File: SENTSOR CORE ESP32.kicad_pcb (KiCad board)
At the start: 2 copper layers, 35.6 x 35.6 mm, 84 parts, among them J1 HYC80-TF08-375, J2 Conn_01x10_Pin, J3 Conn_01x10_Pin, J4 Conn_01x10_Pin, J5 JST_PH 2.0mm, J6 TYPEC-304S-ACP16, Q1 SL8205S, Q2 CJ2301, Q3 UMH3N, SW1 SW_Push, SW2 SW_Push, U1 ESP32-WROOM-32UE, U2 DS3231MZ, U3 XC6220B331MR, U4 XC6220B331MR, U5 BQ27441DRZR-G1B, U6 CN3165, U7 DW01A, U8 USBLC6-2SC6, U9 CH340K

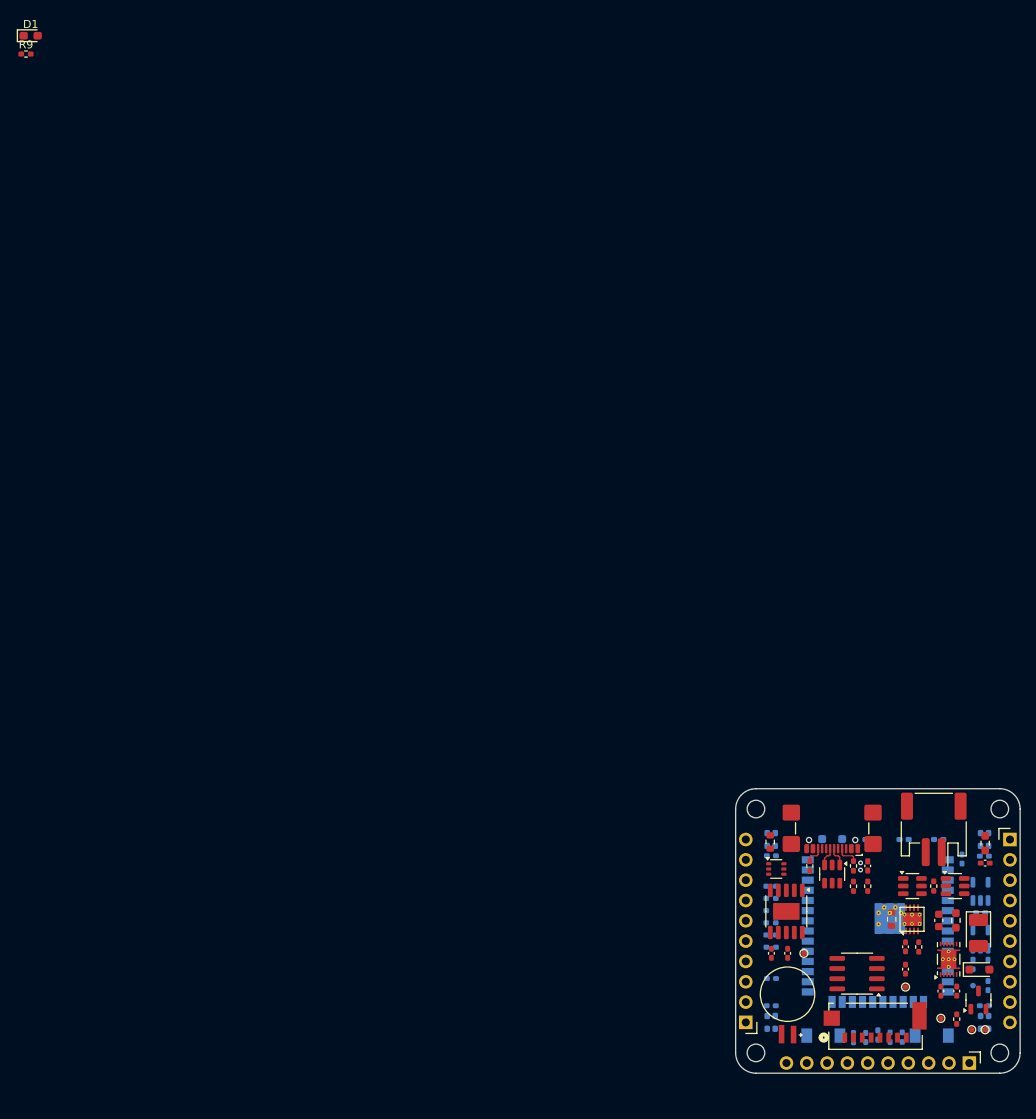
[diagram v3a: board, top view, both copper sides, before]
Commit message: add board layout
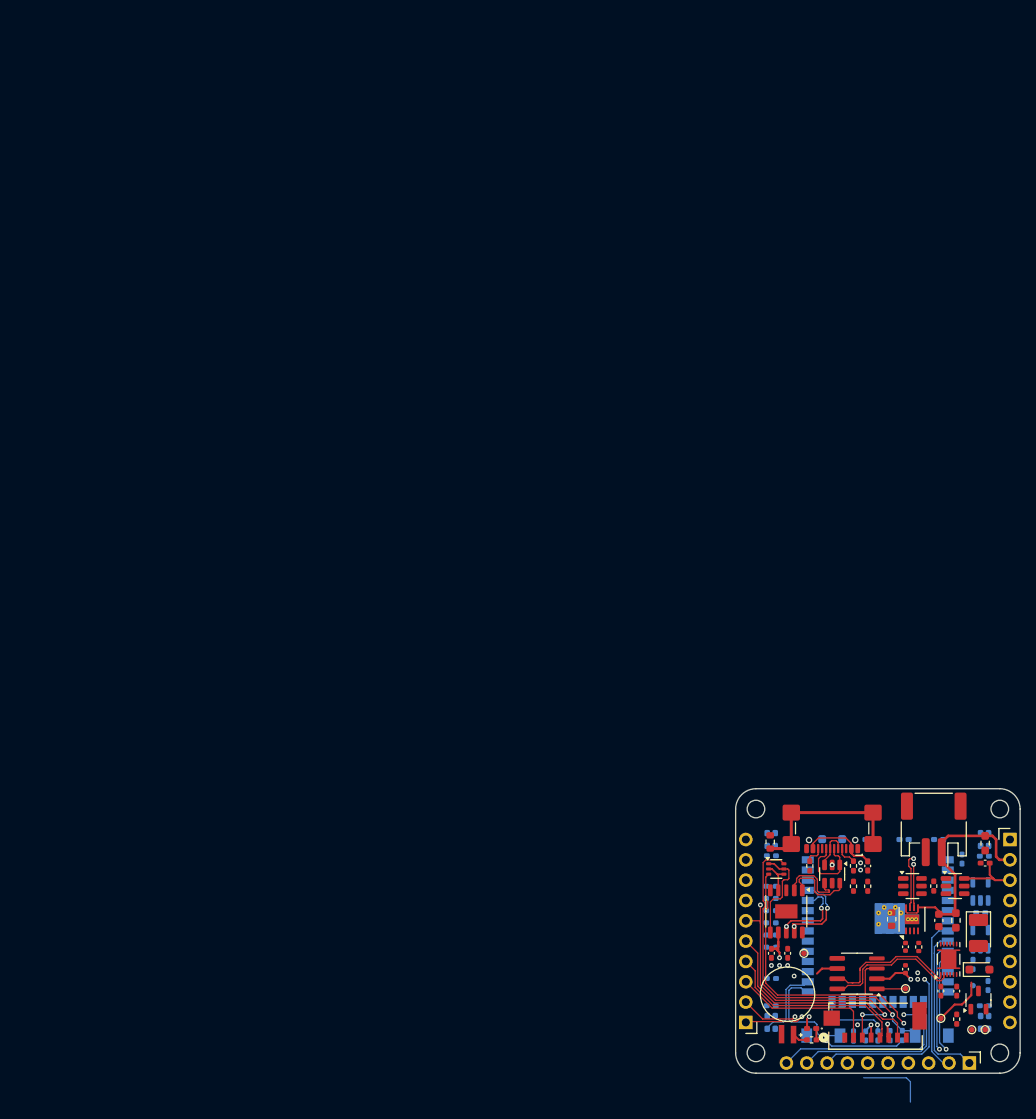
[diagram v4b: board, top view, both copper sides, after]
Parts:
- C18, C4: footprint Capacitor_SMD:C_0402_1005Metric_Pad0.74x0.62mm_HandSolder -> Capacitor_SMD:C_0402_1005Metric
- D1: footprint Diode_SMD:D_0603_1608Metric_Pad1.05x0.95mm_HandSolder -> Diode_SMD:D_0402_1005Metric_Pad0.77x0.64mm_HandSolder
- R12: footprint Resistor_SMD:R_0402_1005Metric_Pad0.72x0.64mm_HandSolder -> Resistor_SMD:R_0402_1005Metric
- moved D1 157.9 mm to (99.3, 124.9), turned to 180 degrees
- moved R9 157.6 mm to (99.3, 126.3)
- moved C3 0.20 mm to (106.1, 125.8)
- moved R1 0.20 mm to (110.7, 125.8)
- moved R16 0.20 mm to (109.1, 125.8)
- moved R2 0.20 mm to (104.6, 125.8)
- moved TP4 0.20 mm to (111.1, 119.9)
- moved D3 0.12 mm to (107.6, 125.8)
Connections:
- Q3 pad 2: /DRT -> /DTR
- Q3 pad 4: /DRT -> /DTR
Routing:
- net /BOOT: track 0.00 -> 52.5 mm, vias 0 -> 1
- net /RST: track 0.00 -> 40.5 mm, vias 0 -> 1
- net /SPI_MOSI: track 0.00 -> 34.9 mm, vias 0 -> 3
- net VBAT0+: track 0.00 -> 29.0 mm
- net /SPI_MISO: track 0.00 -> 27.4 mm
- net /I2C_SCL: track 0.00 -> 24.9 mm, vias 0 -> 1
- net /JTAG_TDI: track 0.00 -> 24.3 mm, vias 0 -> 1
- net /I2C_SDA: track 0.00 -> 24.3 mm, vias 0 -> 1
- net /SPI_SCK: track 0.00 -> 23.4 mm
- net /JTAG_TCK: track 0.00 -> 22.7 mm
- net /JTAG_TMS: track 0.00 -> 22.3 mm, vias 0 -> 1
- net Net-(J6-SHIELD): track 0.00 -> 21.0 mm
- net /IO33: track 0.00 -> 19.9 mm
- net /IO32: track 0.00 -> 19.3 mm
- net /SPI_SS: track 0.00 -> 18.3 mm
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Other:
- copper layers 2 -> 4
- rule pad_to_mask_clearance: 0 -> 0.0254

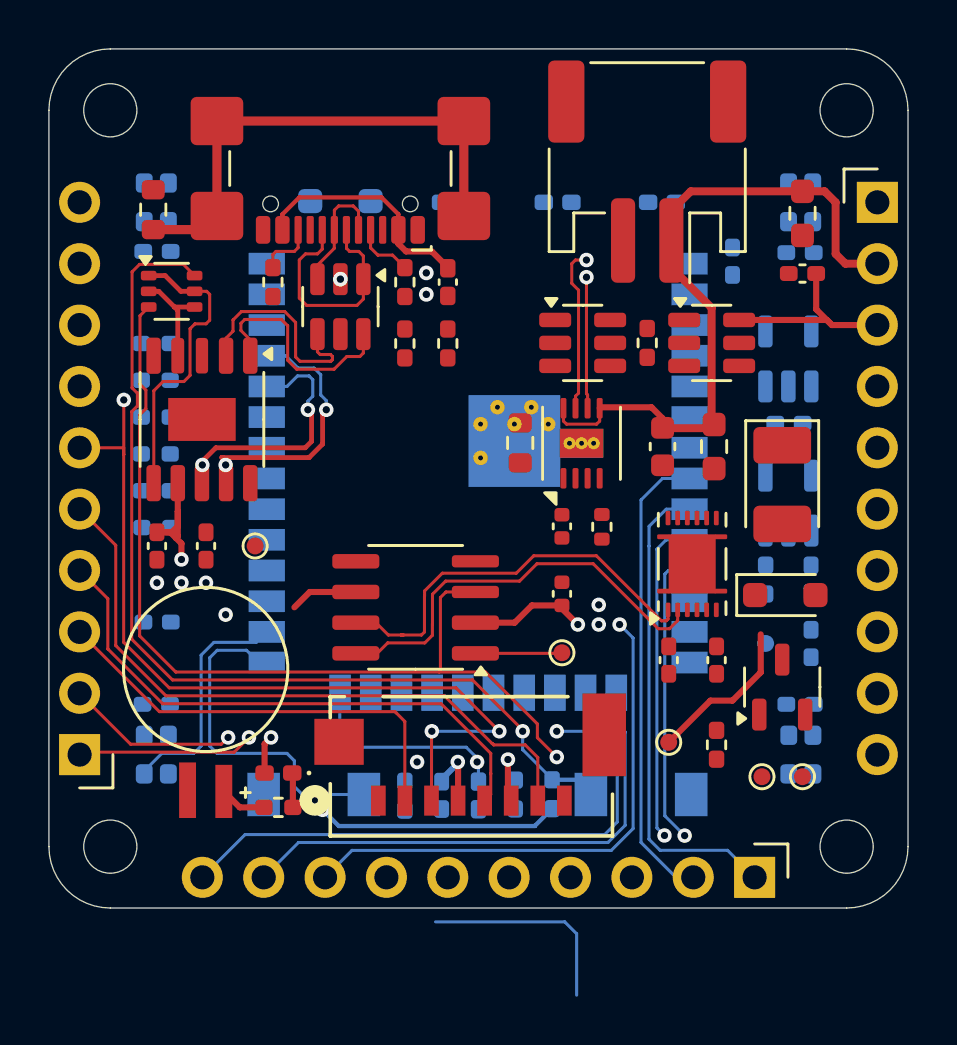
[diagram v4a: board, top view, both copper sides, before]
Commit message: add board layout 85%
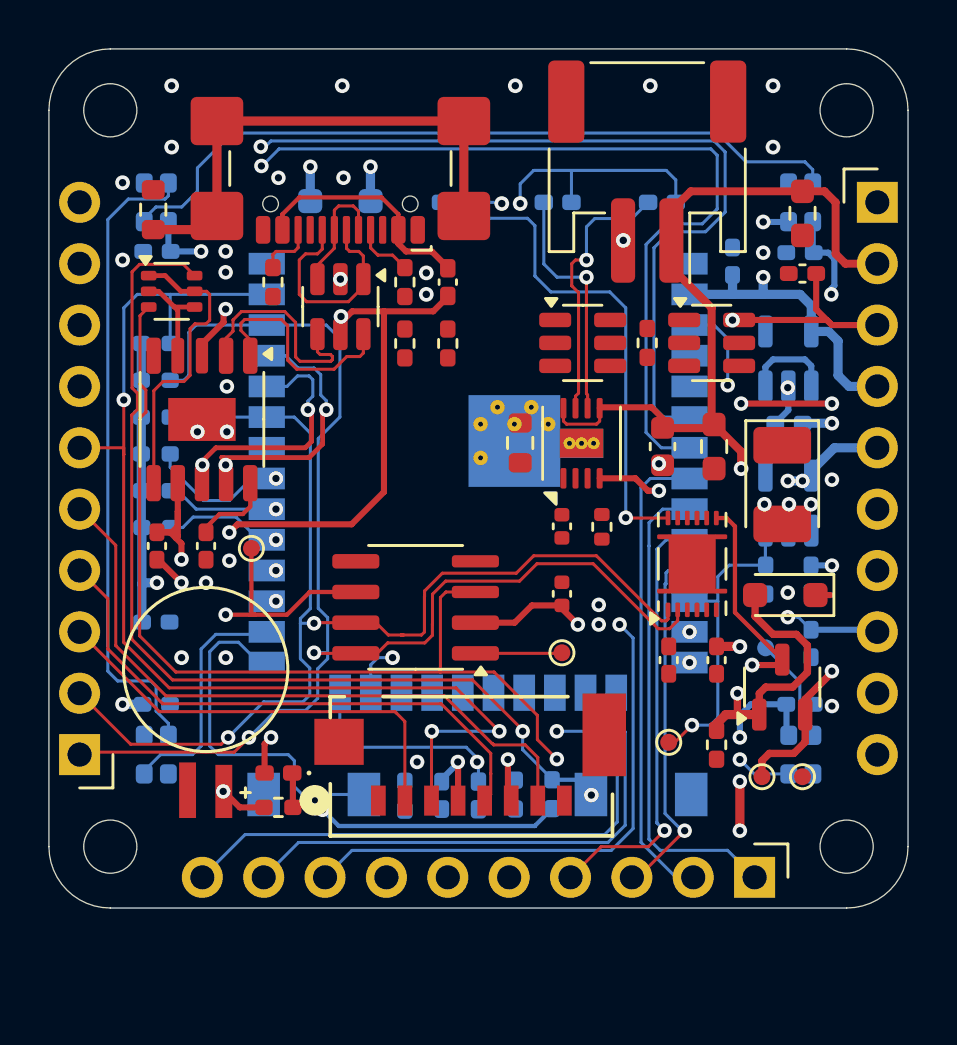
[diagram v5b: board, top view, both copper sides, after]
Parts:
- moved TP1 0.18 mm to (98.2, 115.6)
- moved TP2 0.18 mm to (119.5, 119.7)
- moved C6 0.05 mm to (94.3, 118.6)
- turned C14 to 180 degrees
- turned C15 to 0 degrees
- turned D8 to 180 degrees
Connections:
- R11 pad 1: Net-(U3-CE) -> /LDO_EN
- TP3 pad 1: Net-(U3-CE) -> /LDO_EN
- U3 pad 3: Net-(U3-CE) -> /LDO_EN
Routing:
- net VIN0: track 0.00 -> 73.0 mm, vias 0 -> 5
- net +3V30: track 10.1 -> 68.7 mm, vias 1 -> 4
- net /I35: track 0.00 -> 44.3 mm, vias 0 -> 1
- net /I34: track 0.00 -> 43.2 mm, vias 0 -> 1
- net /RST: track 40.5 -> 75.0 mm, vias 1 -> 4
- net VUSB: track 5.75 -> 36.8 mm, vias 1 -> 4
- net Net-(D5-DOUT): track 0.00 -> 31.0 mm
- net /I2C_SCL: track 24.9 -> 55.5 mm, vias 1 -> 2
- net +3V3: track 9.17 -> 37.0 mm, vias 4 -> 10
- net Net-(D6-DOUT): track 0.00 -> 26.8 mm, vias 0 -> 2
- net Net-(D4-DOUT): track 0.00 -> 26.6 mm
- net /I2C_SDA: track 24.3 -> 47.9 mm, vias 1 -> 2
- net /LED: track 8.98 -> 30.6 mm
- net /GPOUT: track 0.00 -> 21.1 mm, vias 0 -> 1
- net /IO17: track 0.00 -> 20.1 mm, vias 0 -> 1
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
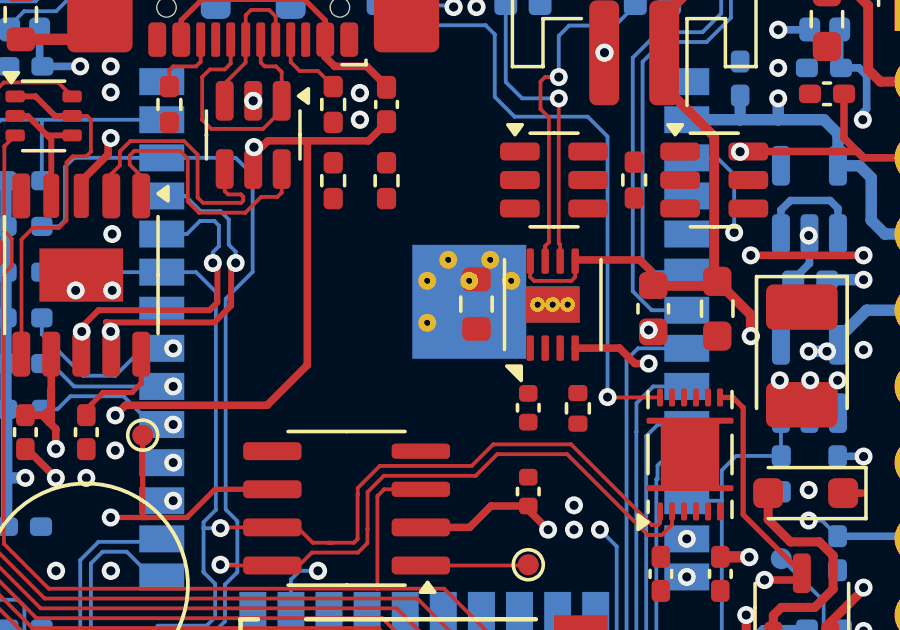
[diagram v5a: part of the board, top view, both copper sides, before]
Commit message: add board layout 85%
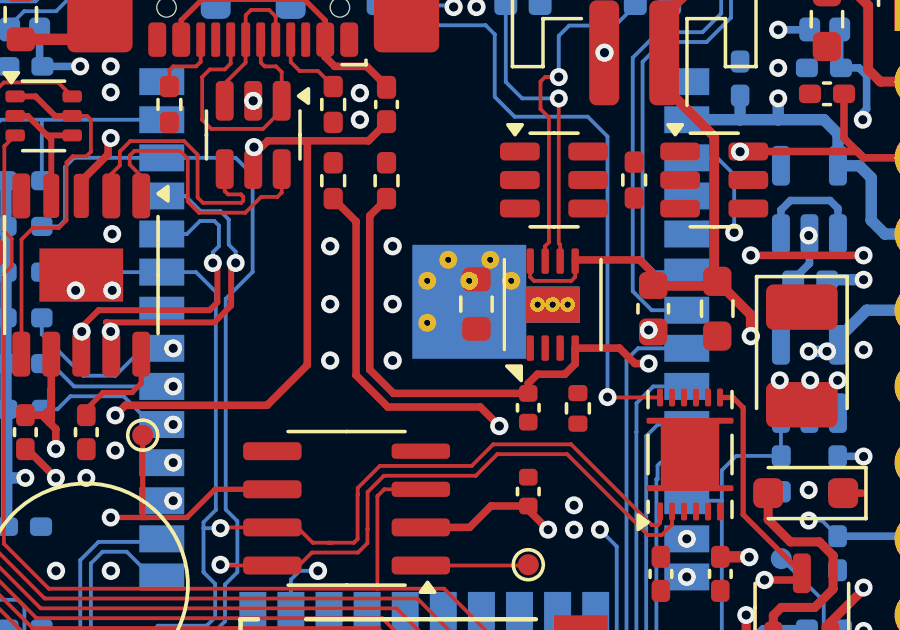
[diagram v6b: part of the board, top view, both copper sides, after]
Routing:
- net VIN0: track 73.0 -> 87.2 mm
- net VBAT+: track 19.7 -> 31.4 mm, vias 2 -> 3
- net GND: vias 36 -> 42
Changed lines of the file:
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@@
 	)
 	(via
+		(at 104.4704 111.2268)
+		(size 0.6096)
+		(drill 0.3048)
+		(layers "F.Cu" "B.Cu")
+		(free yes)
+		(net 1)
+	)
+	(via
 		(at 105.08 124.4348)
 		(size 0.6)
@@
 	)
 	(via
+		(at 104.4704 109.2964)
+		(size 0.6096)
+		(drill 0.3048)
+		(layers "F.Cu" "B.Cu")
+		(free yes)
+		(net 1)
+	)
+	(via
 		(at 95.3264 117.018)
 		(size 0.6)
@@
 	)
 	(via
+		(at 106.5532 113.1064)
+		(size 0.6096)
+		(drill 0.3048)
+		(layers "F.Cu" "B.Cu")
+		(free yes)
+		(net 1)
+	)
+	(via
 		(at 97.1552 105.6896)
 		(size 0.6)
@@
 	)
 	(via
+		(at 106.5532 111.2268)
+		(size 0.6096)
+		(drill 0.3048)
+		(layers "F.Cu" "B.Cu")
+		(free yes)
+		(net 1)
+	)
+	(via
 		(at 119.812 98.984)
 		(size 0.6096)
@@
 	)
 	(via
+		(at 106.5532 109.2964)
+		(size 0.6096)
+		(drill 0.3048)
+		(layers "F.Cu" "B.Cu")
+		(free yes)
+		(net 1)
+	)
+	(via
 		(at 97.206 108.89)
 		(size 0.6)
@@
 	)
 	(via
+		(at 104.4704 113.1064)
+		(size 0.6096)
+		(drill 0.3048)
+		(layers "F.Cu" "B.Cu")
+		(free yes)
+		(net 1)
+	)
+	(via
 		(at 97.3076 116.1036)
 		(size 0.6)
@@
 	)
 	(segment
+		(start 111.3792 113.5636)
+		(end 112.2936 113.5636)
+		(width 0.254)
+		(layer "F.Cu")
+		(net 12)
+	)
+	(segment
+		(start 111.0744 114.2012)
+		(end 111.0744 113.8684)
+		(width 0.254)
+		(layer "F.Cu")
+		(net 12)
+	)
+	(segment
+		(start 106.5812 114.2012)
+		(end 111.0744 114.2012)
+		(width 0.254)
+		(layer "F.Cu")
+		(net 12)
+	)
+	(segment
 		(start 117.4752 123.1261)
 		(end 117.4752 122.86)
@@
 	)
 	(segment
+		(start 105.7912 113.4112)
+		(end 106.5812 114.2012)
+		(width 0.254)
+		(layer "F.Cu")
+		(net 12)
+	)
+	(segment
 		(start 117.4752 122.86)
 		(end 117.8617 122.4735)
@@
 	)
 	(segment
+		(start 111.0744 113.8684)
+		(end 111.3792 113.5636)
+		(width 0.254)
+		(layer "F.Cu")
+		(net 12)
+	)
+	(segment
 		(start 120.6248 121.336)
 		(end 119.5072 121.336)
@@
 	)
 	(segment
+		(start 112.2936 113.5636)
+		(end 112.637 113.2202)
+		(width 0.254)
+		(layer "F.Cu")
+		(net 12)
+	)
+	(segment
+		(start 105.7912 108.2804)
+		(end 105.7912 113.4112)
+		(width 0.254)
+		(layer "F.Cu")
+		(net 12)
+	)
+	(segment
 		(start 117.8617 122.4735)
 		(end 118.3388 122.4735)
@@
 	)
 	(segment
+		(start 106.35 107.7216)
+		(end 105.7912 108.2804)
+		(width 0.254)
+		(layer "F.Cu")
+		(net 12)
+	)
+	(segment
 		(start 119.243 121.6002)
 		(end 119.243 122.4735)
@@
 		(net 12)
 	)
+	(segment
+		(start 112.637 113.2202)
+		(end 112.637 112.693)
+		(width 0.254)
+		(layer "F.Cu")
+		(net 12)
+	)
+	(segment
+		(start 106.35 107.7095)
+		(end 106.35 107.7216)
+		(width 0.254)
+		(layer "F.Cu")
+		(net 12)
+	)
 	(via
 		(at 103.1496 99.7968)
@@
 	)
 	(segment
+		(start 105.334 113.597467)
+		(end 106.392733 114.6562)
+		(width 0.254)
+		(layer "F.Cu")
+		(net 63)
+	)
+	(segment
 		(start 117.894 114.338)
 		(end 118.2372 114.6812)
@@
 	)
 	(segment
+		(start 106.392733 114.6562)
+		(end 109.4746 114.6562)
+		(width 0.254)
+		(layer "F.Cu")
+		(net 63)
+	)
+	(segment
+		(start 105.334 108.4715)
+		(end 105.334 113.597467)
+		(width 0.254)
+		(layer "F.Cu")
+		(net 63)
+	)
+	(segment
 		(start 119.9699 120.4216)
 		(end 120.193 120.1985)
@@
 	)
 	(segment
+		(start 104.572 107.7095)
+		(end 105.334 108.4715)
+		(width 0.254)
+		(layer "F.Cu")
+		(net 63)
+	)
+	(segment
+		(start 109.4746 114.6562)
+		(end 110.1092 115.2908)
+		(width 0.254)
+		(layer "F.Cu")
+		(net 63)
+	)
+	(segment
 		(start 118.2372 114.6812)
 		(end 118.2372 118.2427)
@@
 		(size 0.6096)
 		(drill 0.3048)
+		(layers "F.Cu" "B.Cu")
+		(free yes)
+		(net 63)
+	)
+	(via
+		(at 110.1092 115.2908)
+		(size 0.6096)
+		(drill 0.3048)

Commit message: add board layout 90%
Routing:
- net VBAT-: track 15.6 -> 23.7 mm
- net Net-(D2-A): track 1.39 -> 9.49 mm
- net VIN: track 18.7 -> 26.0 mm
- net Net-(D10-A): track 9.90 -> 16.8 mm
- net Net-(U7-VCC): track 0.00 -> 6.43 mm
- net Net-(U5-BIN): track 0.00 -> 4.37 mm
- net Net-(U6-ISET): track 0.00 -> 4.15 mm
- net VBAT0+: track 39.6 -> 43.7 mm
- net Net-(Q1-G2): track 0.00 -> 3.97 mm
- net Net-(U5-V_{DD}): track 0.00 -> 2.73 mm
- net /I34: track 43.2 -> 45.4 mm
- net /I35: track 44.3 -> 46.5 mm
- net VBAT+: track 31.4 -> 33.5 mm
- net GND: track 7.26 -> 9.24 mm, vias 42 -> 61
- net Net-(U7-CS): track 0.00 -> 1.78 mm
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
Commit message: add board layout 100% first
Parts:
- added G***: LOGO, LOGO, F.Cu at (101.7, 111.1)
- H1, H2, H3, H4: footprint MountingHole:MountingHole_2.2mm_M2 -> MountingHole:MountingHole_2.2mm_M2_Pad_Via
- turned R2 to 90 degrees
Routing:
- net GND: track 9.24 -> 23.3 mm
- net +3V3: track 37.0 -> 41.9 mm
- net VBAT+: track 33.5 -> 38.0 mm
- net Net-(Q1-G1): track 0.00 -> 4.19 mm
- net VIN: track 26.0 -> 29.1 mm
- net /BOOT: track 70.8 -> 73.3 mm, vias 1 -> 2
- net Net-(D3-A): track 0.00 -> 1.53 mm
- net VBAT0+: track 43.7 -> 45.2 mm
- net VIN0: track 87.4 -> 86.1 mm
- net /I2C_SCL: track 55.5 -> 54.4 mm
- net +3V30: track 68.7 -> 69.3 mm
- added copper zone on In1.Cu, net +3V3
- added copper zone on B.Cu, net GND
- added copper zone on F.Cu, net GND
- added copper zone on In2.Cu, net GND
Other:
- board text added: "+"
- board text added: "-"
- board text added: "1S LIPO"
- board text added: "32KHZ"
- board text added: "ALRM"
- board text added: "BOOT"
- board text added: "CHGR"
- board text added: "ESP32-WROOM-32UE"
- board text added: "FULL"
- board text added: "ISET"
- board text added: "LDO_EN"
- board text added: "LED"
- board text added: "OPEN SOURCE HARDWARE"
- board text added: "RESET"
- board text added: "RGB1"
- board text added: "RGB2"
- board text added: "RGB3"
- board text added: "RGB4"
- board text added: "SENTSOR OSHW PROJECT"
